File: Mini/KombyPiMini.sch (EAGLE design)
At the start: 5 parts

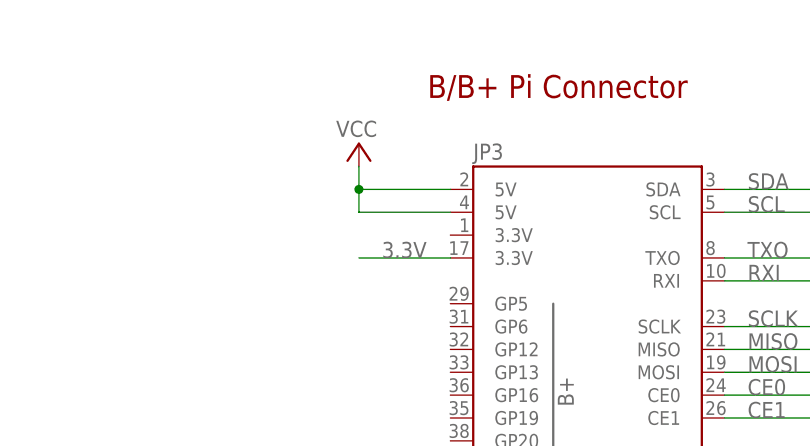
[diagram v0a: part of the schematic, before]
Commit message: Update KombyPiMini with properly oriented nRF
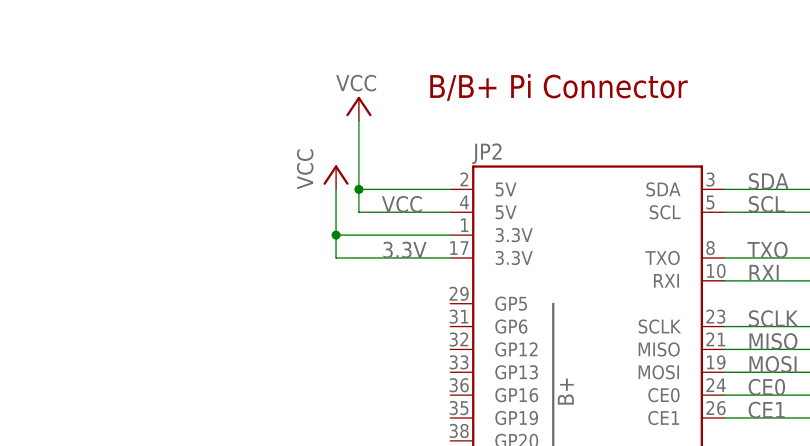
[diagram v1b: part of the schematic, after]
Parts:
- C2: device SparkFun:CAP_POLPTH1 -> rcl:CPOL-USE5-6
- renumbered JP3 to JP2
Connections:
- net 3.3V: now also JP2.3.3V@1
